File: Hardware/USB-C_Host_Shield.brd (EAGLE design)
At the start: 53.3 x 59.7 mm, 47 parts, among them J1 USB-C, J2 GPIN, J3 GPOUT, U1 ARDUINO_UNO_R3_SHIELDBASIC, U2 LM1117, U3 74HC4050, U5 MAX3421, U6 3.3V/150mA, Y1 12.0mhZ

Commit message: Added measurements
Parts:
- moved FRAME1 6.35 mm to (0.00, -31.8)
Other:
- board text added: "M. Chodikov"
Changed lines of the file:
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@@
 <layer number="38" name="bTest" color="7" fill="1" visible="no" active="yes"/>
 <layer number="39" name="tKeepout" color="4" fill="11" visible="no" active="yes"/>
-<layer number="40" name="bKeepout" color="1" fill="11" visible="no" active="yes"/>
+<layer number="40" name="bKeepout" color="1" fill="11" visible="yes" active="yes"/>
 <layer number="41" name="tRestrict" color="4" fill="10" visible="no" active="yes"/>
 <layer number="42" name="bRestrict" color="1" fill="10" visible="no" active="yes"/>
@@
 <dimension x1="45.72" y1="2.54" x2="53.34" y2="3.81" x3="49.53" y3="-13.97" textsize="1.778" textratio="15" layer="48" dtype="horizontal" unit="inch"/>
 <dimension x1="25.4" y1="2.54" x2="27.94" y2="2.54" x3="26.67" y3="-8.89" textsize="1.778" textratio="15" layer="48" dtype="horizontal" unit="inch"/>
+<text x="26.67" y="-31.75" size="1.778" layer="51" font="vector" ratio="10">M. Chodikov</text>
 </plain>
 <attributes>
@@
 <element name="FD3" library="SparkFun-Aesthetics" package="FIDUCIAL-MICRO" value="FIDUCIALUFIDUCIAL" x="46.99" y="57.15" smashed="yes" rot="MR0"/>
 <element name="FD4" library="SparkFun-Aesthetics" package="FIDUCIAL-MICRO" value="FIDUCIALUFIDUCIAL" x="46.99" y="57.15" smashed="yes"/>
-<element name="FRAME1" library="SparkFun-Aesthetics" package="CREATIVE_COMMONS" value="FRAME-LETTER" x="3.81" y="-36.83" smashed="yes">
-<attribute name="DESIGNER" value="" x="83.82" y="-115.57" size="1.778" layer="27" display="off"/>
-<attribute name="REV" value="" x="83.82" y="-115.57" size="1.778" layer="27" display="off"/>
+<element name="FRAME1" library="SparkFun-Aesthetics" package="CREATIVE_COMMONS" value="FRAME-LETTER" x="0" y="-31.75" smashed="yes">
+<attribute name="DESIGNER" value="" x="80.01" y="-110.49" size="1.778" layer="27" display="off"/>
+<attribute name="REV" value="" x="80.01" y="-110.49" size="1.778" layer="27" display="off"/>
 </element>
 <element name="J1" library="SparkFun-Connectors" package="USB-C-16P-2LAYER-PADS" value="USB-C" x="35.56" y="52.07" smashed="yes" rot="R180">

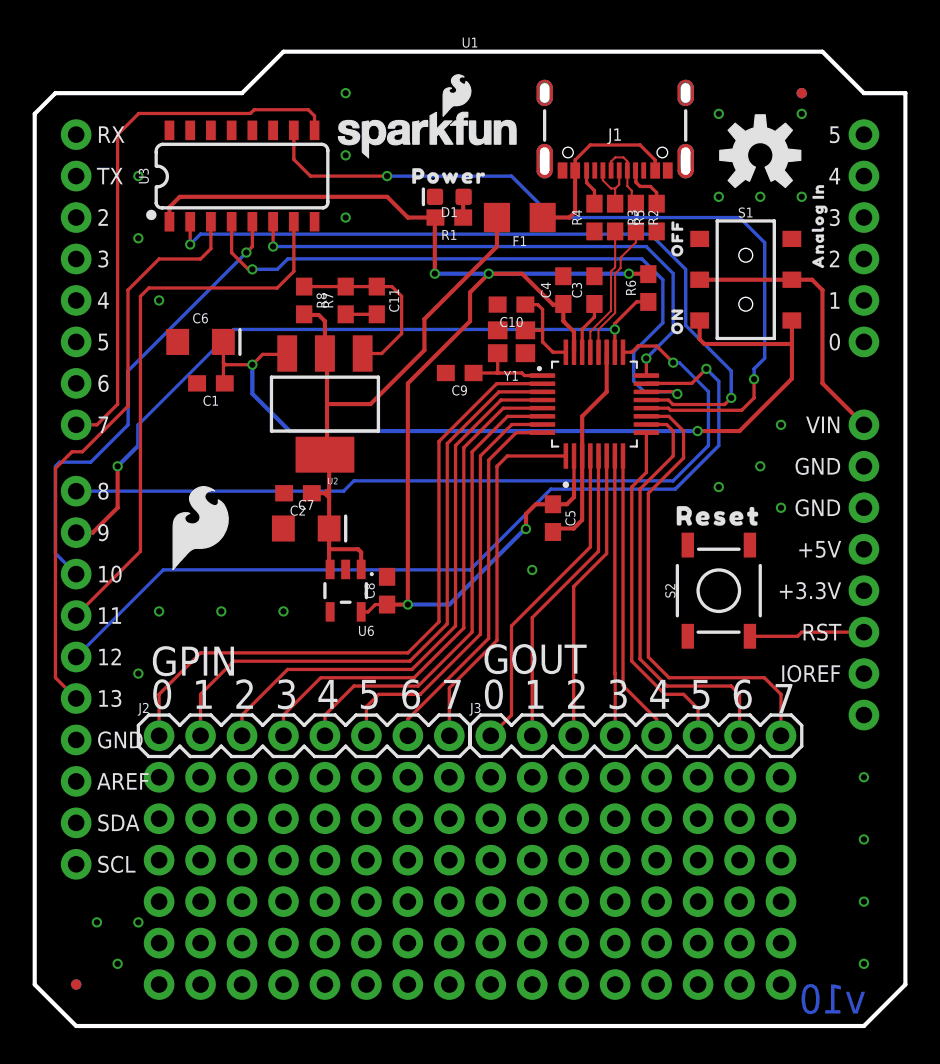
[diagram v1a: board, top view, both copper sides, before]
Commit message: Adjusted design from comments
Added switch in schematic for swap between 5V and VIN from Arduino, added more GND vias and adjusted traces for GND pour, changed schematic tags to flags rather than text, adjusted version number on the back of the board
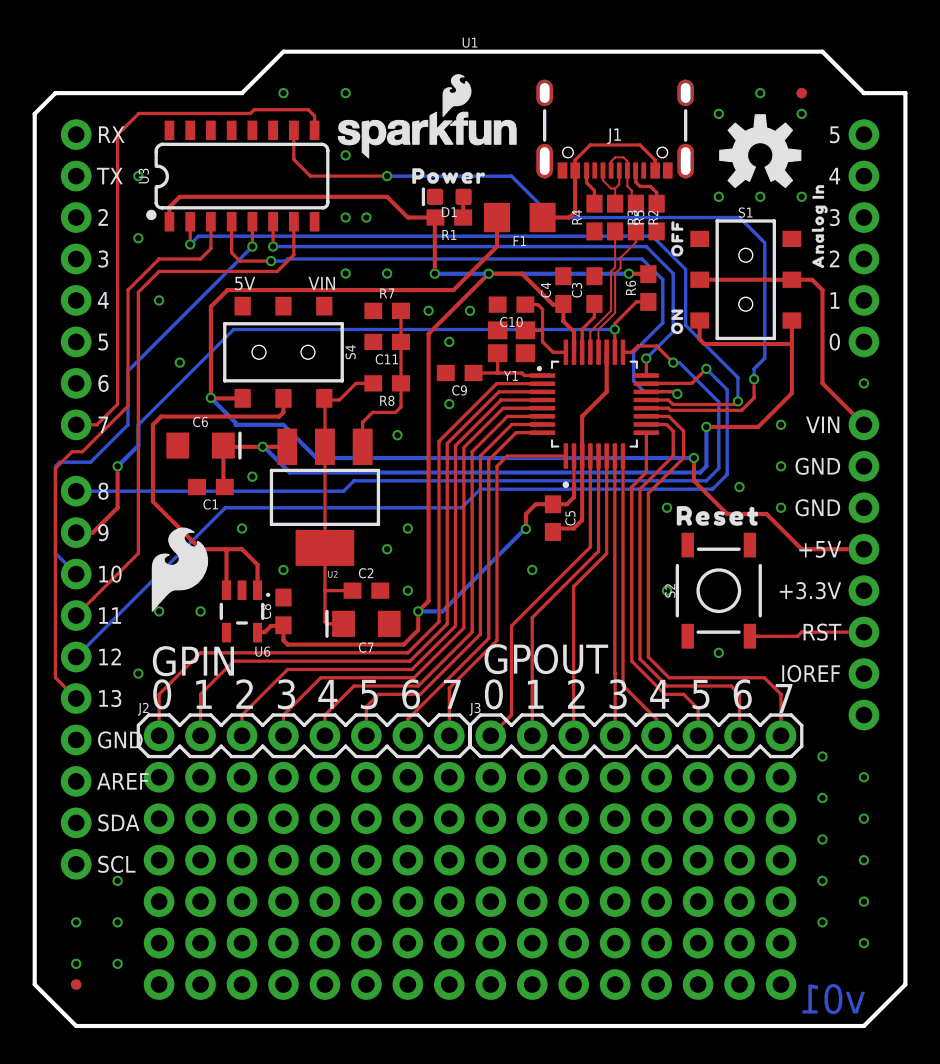
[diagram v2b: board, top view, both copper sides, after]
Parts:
- added S4: Power_Switch, SparkFun-Switches:SWITCH_DPDT_SMD_AYZ0202
- moved C2 7.29 mm to (20.3, 26.7), turned to 0 degrees
- moved R8 7.18 mm to (21.6, 39.4), turned to 180 degrees
- moved C7 6.91 mm to (20.3, 24.6), turned to 180 degrees
- moved U6 6.48 mm to (12.7, 25.4)
- moved C8 6.48 mm to (15.2, 25.4)
- moved C1 6.35 mm to (10.8, 33.0)
- moved C6 6.35 mm to (10.2, 35.6)
- moved U2 5.72 mm to (17.8, 32.4)
- moved U$4 2.84 mm to (8.89, 27.9)
- moved C11 2.62 mm to (21.6, 41.9), turned to 180 degrees
- moved R7 2.62 mm to (21.6, 43.8), turned to 0 degrees
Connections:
- new net N$5: S4.2, U6.1, U6.3
- new net N$6: C2.1, C7.+, R8.2, S4.1, U2.2, U2.4
- net 5V: now also S4.3, U1.5V; no longer C2.1, C7.+, R8.2, U2.2, U2.4, U6.1, U6.3
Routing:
- net 5V: track 39.1 -> 73.1 mm, vias 0 -> 2
- net N$5: track 0.00 -> 26.0 mm
- net N$6: track 0.00 -> 20.0 mm
- net 3.3V: track 84.7 -> 93.7 mm
- net GND: track 14.9 -> 13.0 mm, vias 27 -> 55
- net POCI: track 53.8 -> 55.6 mm
- net GPX: track 49.7 -> 51.5 mm
- net N$4: track 11.4 -> 10.1 mm
- net SCK-IN: track 47.4 -> 48.0 mm
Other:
- board text added: "5V"
- board text added: "GPOUT"
- board text added: "VIN"
- board text added: "v01"
- board text removed: "GOUT"
- board text removed: "v10"

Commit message: Adjusted for design review
Many changes for design have been completed - NOT READY FOR ORDER. See "USB-C PT2" design review document for further information on what needs to be completed.
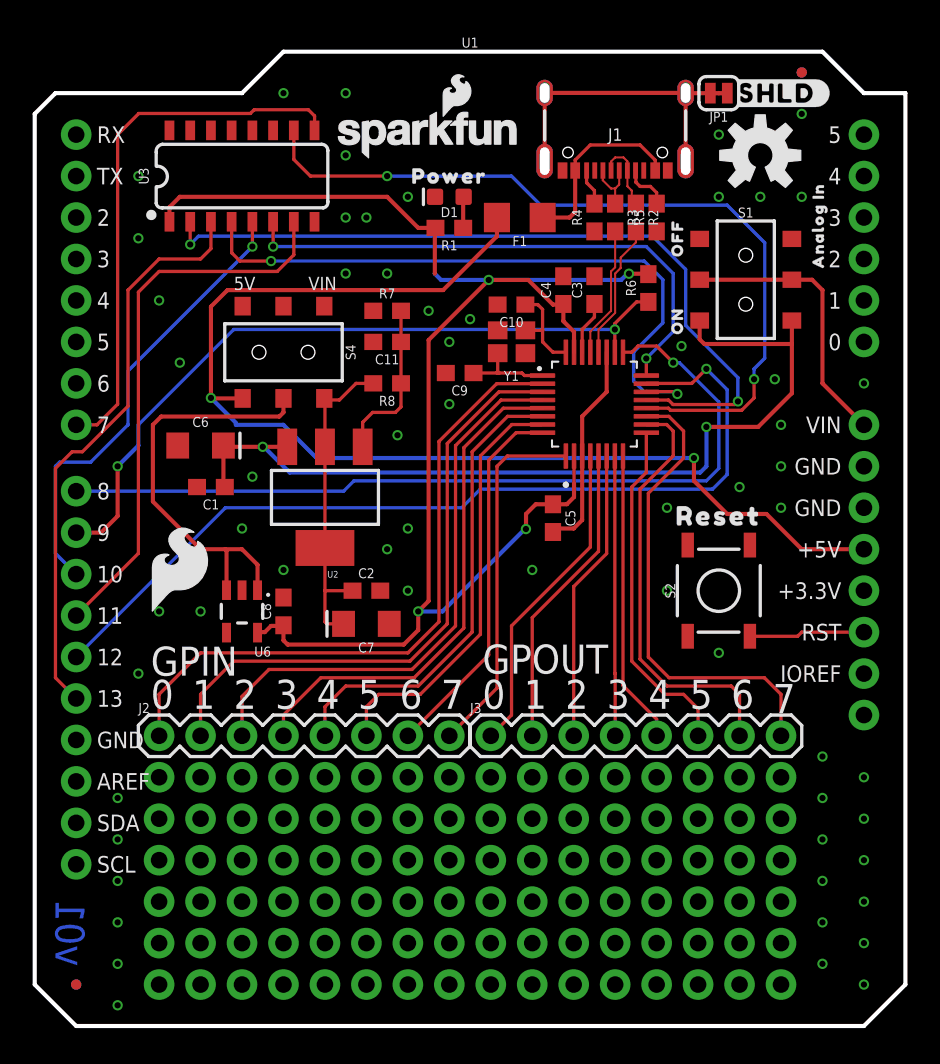
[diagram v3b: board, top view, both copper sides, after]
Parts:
- added JP1: JUMPER-SMT_2_NC_TRACE_SILK, SparkFun-Jumpers:SMT-JUMPER_2_NC_TRACE_SILK
- added U$11: (no value), output:SHLD#33
- moved FD3 1.27 mm to (47.0, 58.4)
- moved FD4 1.27 mm to (47.0, 58.4)
- moved R1 0.63 mm to (25.4, 48.9)
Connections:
- new net N$8: J1.SHLD1, J1.SHLD2, J1.SHLD3, J1.SHLD4, JP1.2
- net GND: now also JP1.1
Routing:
- net N$8: track 0.00 -> 18.5 mm
- net GPIN2: track 34.1 -> 34.8 mm
- net N$7: track 1.28 -> 1.92 mm
- net 3.3V: track 93.7 -> 93.2 mm, vias 5 -> 4
- net GND: vias 55 -> 60

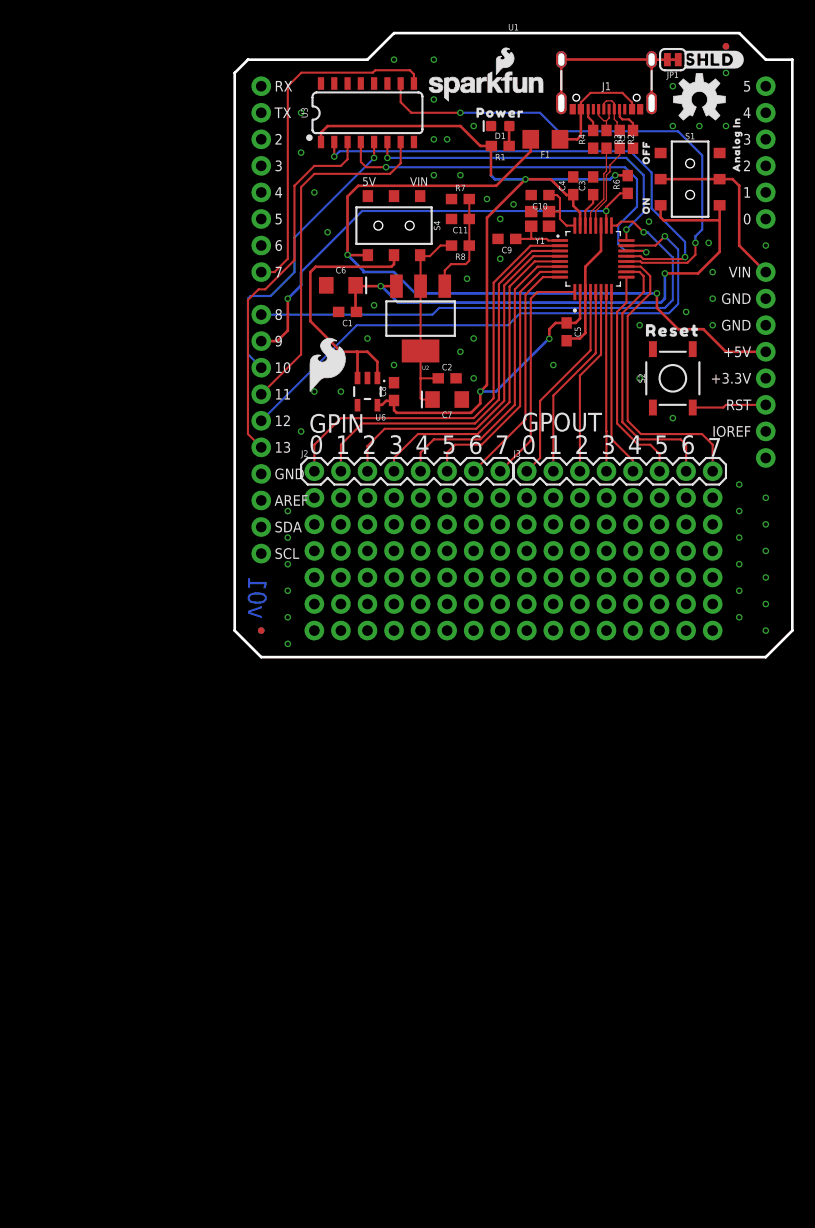
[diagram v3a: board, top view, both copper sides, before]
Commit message: Updates from design review
Adjusted text in schematic to vector font, added pullup resistors to CC1 and CC2, changed power selection and power off section, added lines to silk screen GPIO pins
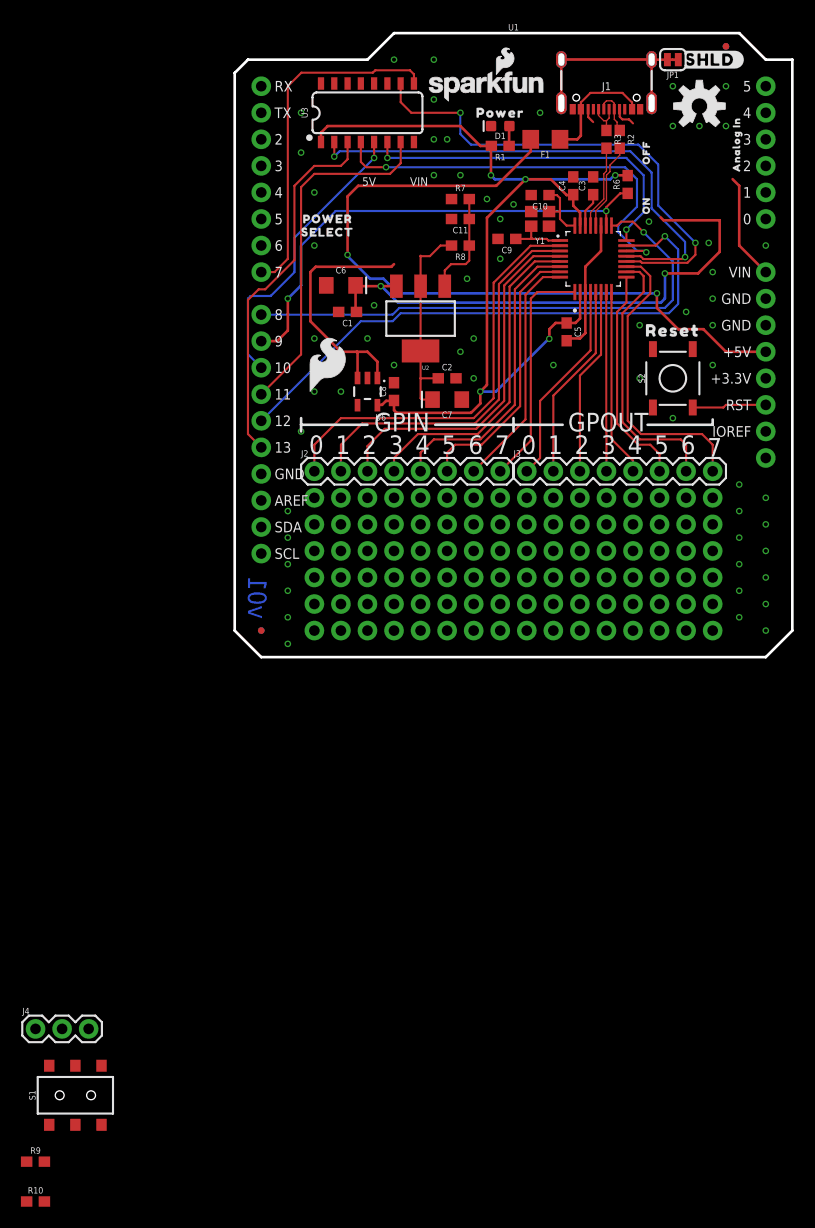
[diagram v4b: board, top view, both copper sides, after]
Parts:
- removed R4, R5: 5.1k, SparkFun-Resistors:0603
- removed S4: Power_Switch, SparkFun-Switches:SWITCH_DPDT_SMD_AYZ0202
- added J4: Power Select, SparkFun-Connectors:1X03
- added R10, R9: 56k, SparkFun-Resistors:0603
- added U$12: (no value), output:POWER38
- added U$13: (no value), output:SELECT37
- S1: value POWER-ON -> (none)
- moved S1 105.5 mm to (-15.2, -41.9), turned to 0 degrees
- moved U$3 0.64 mm to (44.5, 52.7)
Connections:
- removed net N$5: S4.2, U6.1, U6.3
- new net POWER_IN: J4.2, S1.1, S1.2, U6.1, U6.3
- net 5V: now also J4.1, R10.2, R9.2; no longer S4.3
- net CC1: now also R9.1; no longer R5.2
- net CC2: now also R10.1; no longer R4.2
- net GND: no longer R4.1, R5.1
- net N$2: no longer C1.1, C6.+, S1.6, U2.3
- net N$6: now also J4.3; no longer S4.1
- net VIN: now also C1.1, C6.+, U2.3; no longer S1.2, S1.5
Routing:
- net N$2: track 54.5 -> 0.00 mm, vias 2 -> 0
- net VIN: track 17.1 -> 62.1 mm, vias 0 -> 2
- net N$5: track 26.0 -> 0.00 mm
- net POWER_IN: track 0.00 -> 25.1 mm
- net RESET-IN: track 49.5 -> 47.2 mm
- net 5V: track 72.7 -> 70.8 mm
- net INT: track 45.1 -> 46.6 mm
- net CC2: track 2.23 -> 1.43 mm
- net CC1: track 2.94 -> 2.26 mm
- net CS-IN: track 40.9 -> 40.3 mm
- net GND: vias 60 -> 62
- net 3.3V: vias 4 -> 5

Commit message: Continue work with layout
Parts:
- moved R10 114.8 mm to (34.3, 49.5), turned to 270 degrees
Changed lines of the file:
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@@
 <drawing>
 <settings>
-<setting alwaysvectorfont="yes"/>
+<setting alwaysvectorfont="no"/>
 <setting verticaltext="up"/>
 </settings>
@@
 <layer number="44" name="Drills" color="7" fill="1" visible="no" active="yes"/>
 <layer number="45" name="Holes" color="7" fill="1" visible="yes" active="yes"/>
-<layer number="46" name="Milling" color="3" fill="1" visible="yes" active="yes"/>
+<layer number="46" name="Milling" color="3" fill="1" visible="no" active="yes"/>
 <layer number="47" name="Measures" color="7" fill="1" visible="no" active="yes"/>
 <layer number="48" name="Document" color="7" fill="1" visible="no" active="yes"/>
@@
 <attribute name="VALUE" x="-19.05" y="-49.022" size="0.6096" layer="27" font="vector" ratio="20" align="top-center"/>
 </element>
-<element name="R10" library="SparkFun-Resistors" package="0603" value="56k" x="-19.05" y="-52.07" smashed="yes">
-<attribute name="NAME" x="-19.05" y="-51.308" size="0.6096" layer="25" font="vector" ratio="20" align="bottom-center"/>
-<attribute name="VALUE" x="-19.05" y="-52.832" size="0.6096" layer="27" font="vector" ratio="20" align="top-center"/>
+<element name="R10" library="SparkFun-Resistors" package="0603" value="56k" x="34.29" y="49.53" smashed="yes" rot="R270">
+<attribute name="NAME" x="35.052" y="49.53" size="0.6096" layer="25" font="vector" ratio="20" rot="R270" align="bottom-center"/>
+<attribute name="VALUE" x="33.528" y="49.53" size="0.6096" layer="27" font="vector" ratio="20" rot="R270" align="top-center"/>
 </element>
 </elements>
@@
 <wire x1="33.81" y1="51.661" x2="34.29" y2="51.181" width="0.2032" layer="1"/>
 <contactref element="R10" pad="1"/>
-<wire x1="-19.9" y1="-52.07" x2="34.29" y2="51.181" width="0" layer="19" extent="1-1"/>
+<wire x1="34.29" y1="50.38" x2="34.29" y2="51.181" width="0" layer="19" extent="1-1"/>
 </signal>
 <signal name="VBUS">
@@
 <contactref element="R9" pad="2"/>
 <contactref element="R10" pad="2"/>
-<wire x1="-18.2" y1="-48.26" x2="-18.2" y2="-52.07" width="0" layer="19" extent="1-1"/>
+<wire x1="-18.2" y1="-48.26" x2="34.29" y2="48.68" width="0" layer="19" extent="1-1"/>
 <wire x1="-19.05" y1="-35.56" x2="-18.2" y2="-48.26" width="0" layer="19" extent="1-1"/>
 <wire x1="10.826" y1="38.45" x2="-19.05" y2="-35.56" width="0" layer="19" extent="1-1"/>
